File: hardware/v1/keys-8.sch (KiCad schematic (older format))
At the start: 13 parts, among them P1 CONN_02X02, P2 CONN_01X03, P3 CONN_01X03, P4 CONN_01X03, SW1 SWITCH_INV, SW2 SWITCH_INV, SW3 SWITCH_INV, SW4 SWITCH_INV, SW5 SWITCH_INV, SW6 SWITCH_INV, SW7 SWITCH_INV, SW8 SWITCH_INV, U1 MCP23017

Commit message: Re-arrange switch connector pinout to simpler single-row header. Re-route the switch boards accordingly.
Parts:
- removed P1: CONN_02X02, Pin_Headers:Pin_Header_Angled_2x02, symbol CONN_02X02
- added P1: CONN_01X04, Pin_Headers:Pin_Header_Angled_1x04, symbol CONN_01X04
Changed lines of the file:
@@
 LIBS:MCP23017
 LIBS:Pi2_Connector
-LIBS:v1-cache
+LIBS:keys-8-cache
 EELAYER 25 0
 EELAYER END
 $Descr A4 11693 8268
 encoding utf-8
-Sheet 1 27
+Sheet 1 1
 Title ""
 Date ""
@@
 $EndDescr
 $Comp
-L CONN_02X02 P1
-U 1 1 57A4BD78
-P 7000 4750
-F 0 "P1" H 7000 4900 50  0000 C CNN
-F 1 "CONN_02X02" H 7000 4600 50  0000 C CNN
-F 2 "Pin_Headers:Pin_Header_Angled_2x02" H 7000 3550 50  0001 C CNN
-F 3 "" H 7000 3550 50  0000 C CNN
-	1    7000 4750
-	0    -1   -1   0
-$EndComp
-$Comp
 L VDD #PWR01
 U 1 1 57A4BD7F
-P 6900 5500
-F 0 "#PWR01" H 6900 5350 50  0001 C CNN
-F 1 "VDD" H 6900 5650 50  0000 C CNN
-F 2 "" H 6900 5500 50  0000 C CNN
-F 3 "" H 6900 5500 50  0000 C CNN
-	1    6900 5500
-	0    -1   -1   0
+P 7750 4950
+F 0 "#PWR01" H 7750 4800 50  0001 C CNN
+F 1 "VDD" H 7750 5100 50  0000 C CNN
+F 2 "" H 7750 4950 50  0000 C CNN
+F 3 "" H 7750 4950 50  0000 C CNN
+	1    7750 4950
+	1    0    0    -1
 $EndComp
 $Comp
 L GND #PWR02
 U 1 1 57A4BD85
-P 6800 5300
-F 0 "#PWR02" H 6800 5050 50  0001 C CNN
-F 1 "GND" H 6800 5150 50  0000 C CNN
-F 2 "" H 6800 5300 50  0000 C CNN
-F 3 "" H 6800 5300 50  0000 C CNN
-	1    6800 5300
-	0    -1   -1   0
-$EndComp
-Wire Wire Line
-	6800 5300 6800 5000
-Wire Wire Line
-	7050 5000 7050 5500
-Wire Wire Line
-	7050 5500 6900 5500
-Text Label 7050 4500 1    60   ~ 0
+P 8050 4700
+F 0 "#PWR02" H 8050 4450 50  0001 C CNN
+F 1 "GND" H 8050 4550 50  0000 C CNN
+F 2 "" H 8050 4700 50  0000 C CNN
+F 3 "" H 8050 4700 50  0000 C CNN
+	1    8050 4700
+	1    0    0    -1
+$EndComp
+Text Label 8900 5100 2    60   ~ 0
 SDA
-Text Label 6950 4500 1    60   ~ 0
+Text Label 8900 5200 2    60   ~ 0
 SCK
 Text Label 6950 4050 3    60   ~ 0
@@
 	800  4350 800  1600
 Wire Wire Line
-	6800 5000 6950 5000
-Wire Wire Line
 	2600 1600 2600 2100
 Wire Wire Line
@@
 	0    -1   -1   0
 $EndComp
+$Comp
+L CONN_01X04 P1
+U 1 1 57A9C4BF
+P 9100 5050
+F 0 "P1" H 9100 5300 50  0000 C CNN
+F 1 "CONN_01X04" V 9200 5050 50  0000 C CNN
+F 2 "Pin_Headers:Pin_Header_Angled_1x04" H 9100 5050 50  0001 C CNN
+F 3 "" H 9100 5050 50  0000 C CNN
+	1    9100 5050
+	1    0    0    -1
+$EndComp
+Wire Wire Line
+	8050 4700 8900 4700
+Wire Wire Line
+	8900 4700 8900 4900
+Wire Wire Line
+	8900 5000 7750 5000
+Wire Wire Line
+	7750 5000 7750 4950
 $EndSCHEMATC

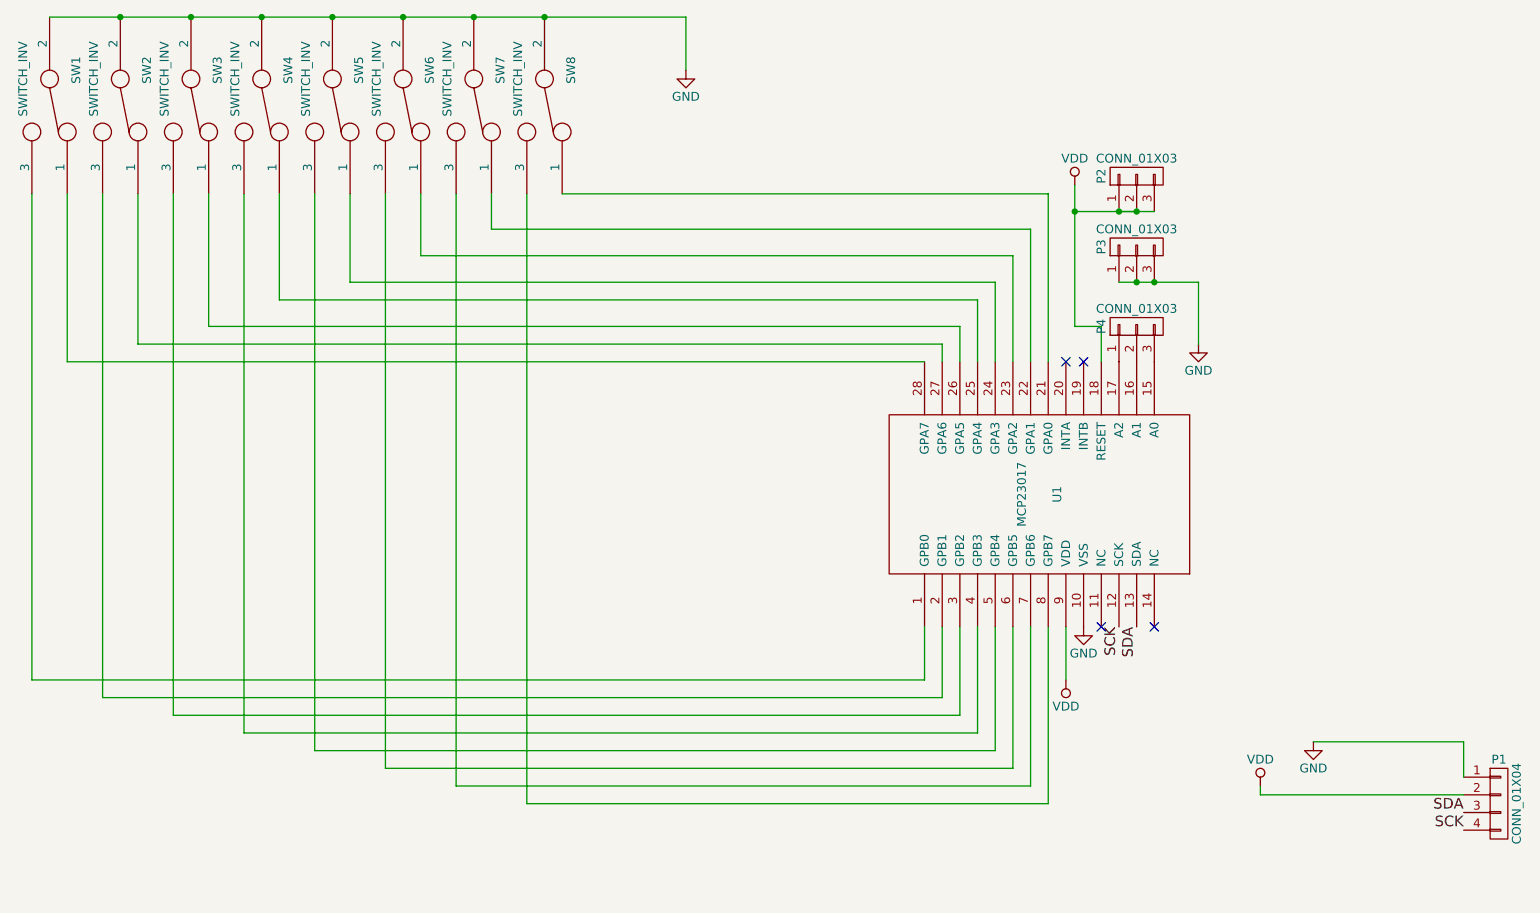
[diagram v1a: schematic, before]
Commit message: Add new schematics for additional switch boards
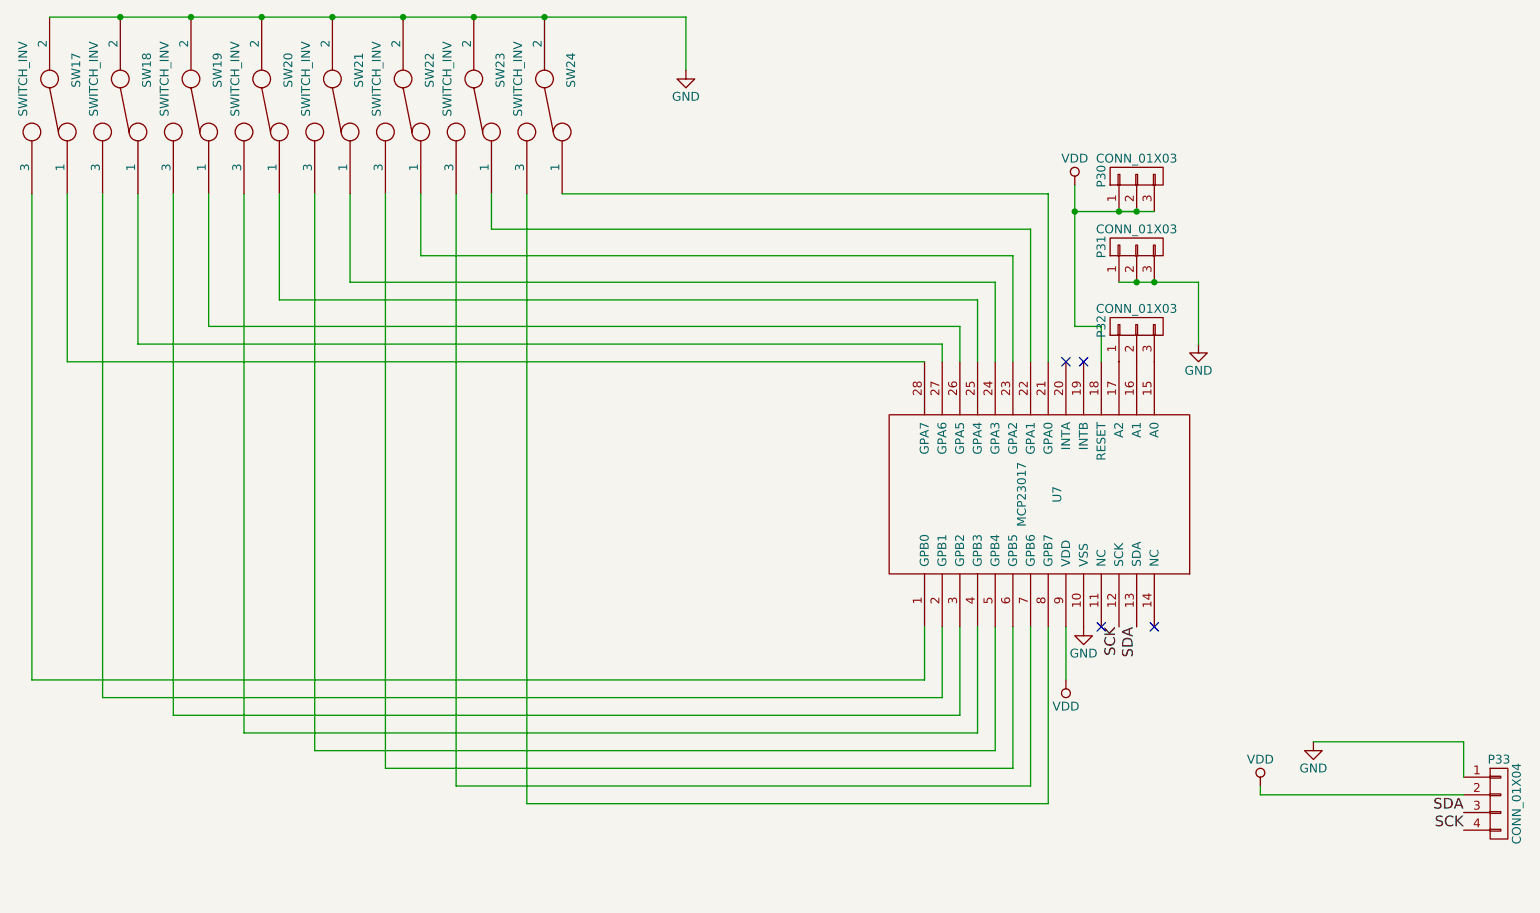
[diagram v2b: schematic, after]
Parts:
- renumbered P2 to P30, P3 to P31, P4 to P32, P1 to P33, SW1 to SW17, SW2 to SW18, SW3 to SW19, SW4 to SW20, SW5 to SW21, SW6 to SW22, SW7 to SW23, SW8 to SW24, U1 to U7
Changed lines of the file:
@@
 LIBS:MCP23017
 LIBS:Pi2_Connector
-LIBS:keys-8-cache
+LIBS:v1-cache
 EELAYER 25 0
 EELAYER END
 $Descr A4 11693 8268
 encoding utf-8
-Sheet 1 1
+Sheet 1 30
 Title ""
 Date ""
@@
 $EndDescr
 $Comp
-L VDD #PWR01
+L VDD #PWR34
 U 1 1 57A4BD7F
 P 7750 4950
-F 0 "#PWR01" H 7750 4800 50  0001 C CNN
+F 0 "#PWR34" H 7750 4800 50  0001 C CNN
 F 1 "VDD" H 7750 5100 50  0000 C CNN
 F 2 "" H 7750 4950 50  0000 C CNN
@@
 $EndComp
 $Comp
-L GND #PWR02
+L GND #PWR35
 U 1 1 57A4BD85
 P 8050 4700
-F 0 "#PWR02" H 8050 4450 50  0001 C CNN
+F 0 "#PWR35" H 8050 4450 50  0001 C CNN
 F 1 "GND" H 8050 4550 50  0000 C CNN
 F 2 "" H 8050 4700 50  0000 C CNN
@@
 NoConn ~ 7150 4050
 $Comp
-L VDD #PWR03
+L VDD #PWR31
 U 1 1 57A4BE5B
 P 6700 1550
-F 0 "#PWR03" H 6700 1400 50  0001 C CNN
+F 0 "#PWR31" H 6700 1400 50  0001 C CNN
 F 1 "VDD" H 6700 1700 50  0000 C CNN
 F 2 "" H 6700 1550 50  0000 C CNN
@@
 	6850 2350 6850 2550
 $Comp
-L GND #PWR04
+L GND #PWR33
 U 1 1 57A4BFF8
 P 7400 2450
-F 0 "#PWR04" H 7400 2200 50  0001 C CNN
+F 0 "#PWR33" H 7400 2200 50  0001 C CNN
 F 1 "GND" H 7400 2300 50  0000 C CNN
 F 2 "" H 7400 2450 50  0000 C CNN
@@
 $EndComp
 $Comp
-L CONN_01X03 P4
+L CONN_01X03 P32
 U 1 1 57A4C019
 P 7050 2350
-F 0 "P4" H 7050 2550 50  0000 C CNN
+F 0 "P32" H 7050 2550 50  0000 C CNN
 F 1 "CONN_01X03" V 7150 2350 50  0000 C CNN
 F 2 "Pin_Headers:Pin_Header_Straight_1x03" H 7050 2350 50  0001 C CNN
@@
 $EndComp
 $Comp
-L CONN_01X03 P3
+L CONN_01X03 P31
 U 1 1 57A4C046
 P 7050 1900
-F 0 "P3" H 7050 2100 50  0000 C CNN
+F 0 "P31" H 7050 2100 50  0000 C CNN
 F 1 "CONN_01X03" V 7150 1900 50  0000 C CNN
 F 2 "Pin_Headers:Pin_Header_Straight_1x03" H 7050 1900 50  0001 C CNN
@@
 $EndComp
 $Comp
-L CONN_01X03 P2
+L CONN_01X03 P30
 U 1 1 57A4C069
 P 7050 1500
-F 0 "P2" H 7050 1700 50  0000 C CNN
+F 0 "P30" H 7050 1700 50  0000 C CNN
 F 1 "CONN_01X03" V 7150 1500 50  0000 C CNN
 F 2 "Pin_Headers:Pin_Header_Straight_1x03" H 7050 1500 50  0001 C CNN
@@
 Connection ~ 7050 2100
 $Comp
-L GND #PWR05
+L GND #PWR32
 U 1 1 57A4C366
 P 6750 4050
-F 0 "#PWR05" H 6750 3800 50  0001 C CNN
+F 0 "#PWR32" H 6750 3800 50  0001 C CNN
 F 1 "GND" H 6750 3900 50  0000 C CNN
 F 2 "" H 6750 4050 50  0000 C CNN
@@
 $EndComp
 $Comp
-L VDD #PWR06
+L VDD #PWR30
 U 1 1 57A4C380
 P 6650 4350
-F 0 "#PWR06" H 6650 4200 50  0001 C CNN
+F 0 "#PWR30" H 6650 4200 50  0001 C CNN
 F 1 "VDD" H 6650 4500 50  0000 C CNN
 F 2 "" H 6650 4350 50  0000 C CNN
@@
 	6650 4050 6650 4350
 $Comp
-L SWITCH_INV SW1
+L SWITCH_INV SW17
 U 1 1 57A4C3BE
 P 900 1100
-F 0 "SW1" H 700 1250 50  0000 C CNN
+F 0 "SW17" H 700 1250 50  0000 C CNN
 F 1 "SWITCH_INV" H 750 950 50  0000 C CNN
 F 2 "myparts:SW_SPDT-custom" H 900 1100 50  0001 C CNN
@@
 $EndComp
 $Comp
-L SWITCH_INV SW2
+L SWITCH_INV SW18
 U 1 1 57A4C448
 P 1300 1100
-F 0 "SW2" H 1100 1250 50  0000 C CNN
+F 0 "SW18" H 1100 1250 50  0000 C CNN
 F 1 "SWITCH_INV" H 1150 950 50  0000 C CNN
 F 2 "myparts:SW_SPDT-custom" H 1300 1100 50  0001 C CNN
@@
 $EndComp
 $Comp
-L SWITCH_INV SW3
+L SWITCH_INV SW19
 U 1 1 57A4C471
 P 1700 1100
-F 0 "SW3" H 1500 1250 50  0000 C CNN
+F 0 "SW19" H 1500 1250 50  0000 C CNN
 F 1 "SWITCH_INV" H 1550 950 50  0000 C CNN
 F 2 "myparts:SW_SPDT-custom" H 1700 1100 50  0001 C CNN
@@
 $EndComp
 $Comp
-L SWITCH_INV SW4
+L SWITCH_INV SW20
 U 1 1 57A4C49D
 P 2100 1100
-F 0 "SW4" H 1900 1250 50  0000 C CNN
+F 0 "SW20" H 1900 1250 50  0000 C CNN
 F 1 "SWITCH_INV" H 1950 950 50  0000 C CNN
 F 2 "myparts:SW_SPDT-custom" H 2100 1100 50  0001 C CNN
@@
 $EndComp
 $Comp
-L SWITCH_INV SW5
+L SWITCH_INV SW21
 U 1 1 57A4C5B0
 P 2500 1100
-F 0 "SW5" H 2300 1250 50  0000 C CNN
+F 0 "SW21" H 2300 1250 50  0000 C CNN
 F 1 "SWITCH_INV" H 2350 950 50  0000 C CNN
 F 2 "myparts:SW_SPDT-custom" H 2500 1100 50  0001 C CNN
@@
 $EndComp
 $Comp
-L SWITCH_INV SW6
+L SWITCH_INV SW22
 U 1 1 57A4C5B6
 P 2900 1100
-F 0 "SW6" H 2700 1250 50  0000 C CNN
+F 0 "SW22" H 2700 1250 50  0000 C CNN
 F 1 "SWITCH_INV" H 2750 950 50  0000 C CNN
 F 2 "myparts:SW_SPDT-custom" H 2900 1100 50  0001 C CNN
@@
 $EndComp
 $Comp
-L SWITCH_INV SW7
+L SWITCH_INV SW23
 U 1 1 57A4C5BC
 P 3300 1100
-F 0 "SW7" H 3100 1250 50  0000 C CNN
+F 0 "SW23" H 3100 1250 50  0000 C CNN
 F 1 "SWITCH_INV" H 3150 950 50  0000 C CNN
 F 2 "myparts:SW_SPDT-custom" H 3300 1100 50  0001 C CNN
@@
 $EndComp
 $Comp
-L SWITCH_INV SW8
+L SWITCH_INV SW24
 U 1 1 57A4C5C2
 P 3700 1100
-F 0 "SW8" H 3500 1250 50  0000 C CNN
+F 0 "SW24" H 3500 1250 50  0000 C CNN
 F 1 "SWITCH_INV" H 3550 950 50  0000 C CNN
 F 2 "myparts:SW_SPDT-custom" H 3700 1100 50  0001 C CNN
@@
 Connection ~ 3700 600
 $Comp
-L GND #PWR07
+L GND #PWR29
 U 1 1 57A4D371
 P 4500 900
-F 0 "#PWR07" H 4500 650 50  0001 C CNN
+F 0 "#PWR29" H 4500 650 50  0001 C CNN
 F 1 "GND" H 4500 750 50  0000 C CNN
 F 2 "" H 4500 900 50  0000 C CNN
@@
 $EndComp
 $Comp
-L MCP23017 U1
+L MCP23017 U7
 U 1 1 57A4B36E
 P 6500 3300
-F 0 "U1" H 6500 3200 50  0000 C CNN
+F 0 "U7" H 6500 3200 50  0000 C CNN
 F 1 "MCP23017" H 6500 3400 50  0000 C CNN
 F 2 "DIL28:DIL28" H 6500 3300 50  0001 C CNN
@@
 $EndComp
 $Comp
-L CONN_01X04 P1
+L CONN_01X04 P33
 U 1 1 57A9C4BF
 P 9100 5050
-F 0 "P1" H 9100 5300 50  0000 C CNN
+F 0 "P33" H 9100 5300 50  0000 C CNN
 F 1 "CONN_01X04" V 9200 5050 50  0000 C CNN
 F 2 "Pin_Headers:Pin_Header_Angled_1x04" H 9100 5050 50  0001 C CNN
